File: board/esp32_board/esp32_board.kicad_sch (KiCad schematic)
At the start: 3 parts, among them J1 Screw_Terminal_01x19, J2 Screw_Terminal_01x19, U1 ESP32-DevKitC

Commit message: feat: Updated board
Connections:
- net 3V3: now reaches U1.1 (3V3)
- net 3V3: now also J2.1 (Pin_1)
- net 26: now reaches U1.10 (DAC_2/ADC2_CH9/GPIO26)
- net 26: now also J2.10 (Pin_10)
- net 27: now reaches U1.11 (ADC2_CH7/GPIO27)
- net 27: now also J2.11 (Pin_11)
- net 14: now reaches U1.12 (MTMS/GPIO14/ADC2_CH6)
- net 14: now also J2.12 (Pin_12)
- net 12: now reaches U1.13 (MTDI/GPIO12/ADC2_CH5)
- net 12: now also J2.13 (Pin_13)
- net GND: now reaches U1.14 (GND), U1.32 (GND), U1.38 (GND)
- net GND: now also J1.1 (Pin_1), J1.7 (Pin_7), J2.14 (Pin_14)
- net 13: now reaches U1.15 (MTCK/GPIO13/ADC2_CH4)
- net 13: now also J2.15 (Pin_15)
- net SD2: now reaches U1.16 (SD_DATA2/GPIO9)
- net SD2: now also J2.16 (Pin_16)
- net SD3: now reaches U1.17 (SD_DATA3/GPIO10)
- net SD3: now also J2.17 (Pin_17)
- net CMD: now reaches U1.18 (CMD)
- net CMD: now also J2.18 (Pin_18)
- net V5: now reaches U1.19 (5V)
- net V5: now also J2.19 (Pin_19)
- net EN: now reaches U1.2 (CHIP_PU)
- net EN: now also J2.2 (Pin_2)
- net CLK: now reaches U1.20 (SD_CLK/GPIO6)
- net CLK: now also J1.19 (Pin_19)
- net SD0: now reaches U1.21 (SD_DATA0/GPIO7)
- net SD0: now also J1.18 (Pin_18)
- net SD1: now reaches U1.22 (SD_DATA1/GPIO8)
- net SD1: now also J1.17 (Pin_17)
- net 15: now reaches U1.23 (MTDO/GPIO15/ADC2_CH3)
- net 15: now also J1.16 (Pin_16)
- net 2: now reaches U1.24 (ADC2_CH2/GPIO2)
- net 2: now also J1.15 (Pin_15)
- net 0: now reaches U1.25 (GPIO0/BOOT/ADC2_CH1)
- net 0: now also J1.14 (Pin_14)
- net 4: now reaches U1.26 (ADC2_CH0/GPIO4)
- net 4: now also J1.13 (Pin_13)
- net 16: now reaches U1.27 (GPIO16)
- net 16: now also J1.12 (Pin_12)
- net 17: now reaches U1.28 (GPIO17)
- net 17: now also J1.11 (Pin_11)
- net 5: now reaches U1.29 (GPIO5)
- net 5: now also J1.10 (Pin_10)
- net SP: now reaches U1.3 (SENSOR_VP/GPIO36/ADC1_CH0)
- net SP: now also J2.3 (Pin_3)
- net 18: now reaches U1.30 (GPIO18)
- net 18: now also J1.9 (Pin_9)
- net 19: now reaches U1.31 (GPIO19)
- net 19: now also J1.8 (Pin_8)
- net 21: now reaches U1.33 (GPIO21)
- net 21: now also J1.6 (Pin_6)
- net RX: now reaches U1.34 (U0RXD/GPIO3)
- net RX: now also J1.5 (Pin_5)
- net TX: now reaches U1.35 (U0TXD/GPIO1)
- net TX: now also J1.4 (Pin_4)
- net 22: now reaches U1.36 (GPIO22)
- net 22: now also J1.3 (Pin_3)
- net 23: now reaches U1.37 (GPIO23)
- net 23: now also J1.2 (Pin_2)
- net SN: now reaches U1.4 (SENSOR_VN/GPIO39/ADC1_CH3)
- net SN: now also J2.4 (Pin_4)
- net 34: now reaches U1.5 (VDET_1/GPIO34/ADC1_CH6)
- net 34: now also J2.5 (Pin_5)
- net 35: now reaches U1.6 (VDET_2/GPIO35/ADC1_CH7)
- net 35: now also J2.6 (Pin_6)
- net 32: now reaches U1.7 (32K_XP/GPIO32/ADC1_CH4)
- net 32: now also J2.7 (Pin_7)
- net 33: now reaches U1.8 (32K_XN/GPIO33/ADC1_CH5)
- net 33: now also J2.8 (Pin_8)
- net 25: now reaches U1.9 (DAC_1/ADC2_CH8/GPIO25)
- net 25: now also J2.9 (Pin_9)

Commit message: feat: Updated presentation and board
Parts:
- J1, J2: footprint (none) -> Connector_PinHeader_2.54mm:PinHeader_1x19_P2.54mm_Vertical
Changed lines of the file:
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@@
 			)
 		)
-		(property "Footprint" ""
+		(property "Footprint" "Connector_PinHeader_2.54mm:PinHeader_1x19_P2.54mm_Vertical"
 			(at 226.06 86.36 0)
 			(effects
@@
 			)
 		)
-		(property "Footprint" ""
+		(property "Footprint" "Connector_PinHeader_2.54mm:PinHeader_1x19_P2.54mm_Vertical"
 			(at 73.66 86.36 0)
 			(effects

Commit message: feat: Updated board
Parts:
- added J3, J5: Conn_01x19_Socket, Connector_PinSocket_2.54mm:PinSocket_1x19_P2.54mm_Vertical, symbol Connector:Conn_01x19_Socket
- added J4, J6: Conn_01x19_Pin, Connector_PinSocket_2.54mm:PinSocket_1x19_P2.54mm_Vertical, symbol Connector:Conn_01x19_Pin
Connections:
- net 0: now also J5.14 (Pin_14), J6.14 (Pin_14)
- net 12: now also J3.13 (Pin_13), J4.13 (Pin_13)
- net 13: now also J3.15 (Pin_15), J4.15 (Pin_15)
- net 14: now also J3.12 (Pin_12), J4.12 (Pin_12)
- net 15: now also J5.16 (Pin_16), J6.16 (Pin_16)
- net 16: now also J5.12 (Pin_12), J6.12 (Pin_12)
- net 17: now also J5.11 (Pin_11), J6.11 (Pin_11)
- net 18: now also J5.9 (Pin_9), J6.9 (Pin_9)
- net 19: now also J5.8 (Pin_8), J6.8 (Pin_8)
- net 2: now also J5.15 (Pin_15), J6.15 (Pin_15)
- net 21: now also J5.6 (Pin_6), J6.6 (Pin_6)
- net 22: now also J5.3 (Pin_3), J6.3 (Pin_3)
- net 23: now also J5.2 (Pin_2), J6.2 (Pin_2)
- net 25: now also J3.9 (Pin_9), J4.9 (Pin_9)
- net 26: now also J3.10 (Pin_10), J4.10 (Pin_10)
- net 27: now also J3.11 (Pin_11), J4.11 (Pin_11)
- net 32: now also J3.7 (Pin_7), J4.7 (Pin_7)
- net 33: now also J3.8 (Pin_8), J4.8 (Pin_8)
- net 34: now also J3.5 (Pin_5), J4.5 (Pin_5)
- net 35: now also J3.6 (Pin_6), J4.6 (Pin_6)
- net 3V3: now also J3.1 (Pin_1), J4.1 (Pin_1)
- net 4: now also J5.13 (Pin_13), J6.13 (Pin_13)
- net 5: now also J5.10 (Pin_10), J6.10 (Pin_10)
- net CLK: now also J5.19 (Pin_19), J6.19 (Pin_19)
- net CMD: now also J3.18 (Pin_18), J4.18 (Pin_18)
- net EN: now also J3.2 (Pin_2), J4.2 (Pin_2)
- net GND: now also J3.14 (Pin_14), J4.14 (Pin_14), J5.1 (Pin_1), J5.7 (Pin_7), J6.1 (Pin_1), J6.7 (Pin_7)
- net RX: now also J5.5 (Pin_5), J6.5 (Pin_5)
- net SD0: now also J5.18 (Pin_18), J6.18 (Pin_18)
- net SD1: now also J5.17 (Pin_17), J6.17 (Pin_17)
- net SD2: now also J3.16 (Pin_16), J4.16 (Pin_16)
- net SD3: now also J3.17 (Pin_17), J4.17 (Pin_17)
- net SN: now also J3.4 (Pin_4), J4.4 (Pin_4)
- net SP: now also J3.3 (Pin_3), J4.3 (Pin_3)
- net TX: now also J5.4 (Pin_4), J6.4 (Pin_4)
- net V5: now also J3.19 (Pin_19), J4.19 (Pin_19)
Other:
- moved on the sheet: J1, J2

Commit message: feat: Updated board and presentation
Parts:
- added H1, H2, H3: MountingHole, symbol Mechanical:MountingHole
- added K1, K2, K3: Relay_SPST-NO, symbol Relay:Relay_SPST-NO
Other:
- moved on the sheet: J1, J2, J3, J4, J5, J6, U1

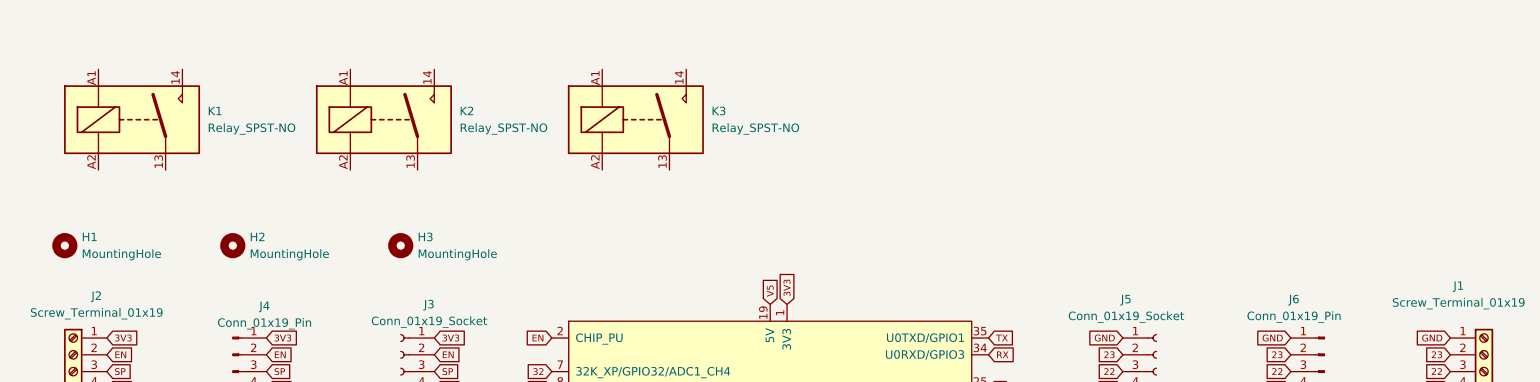
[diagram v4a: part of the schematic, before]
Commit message: feat(board): Added modules - gps, compass, relay. And builded schematic
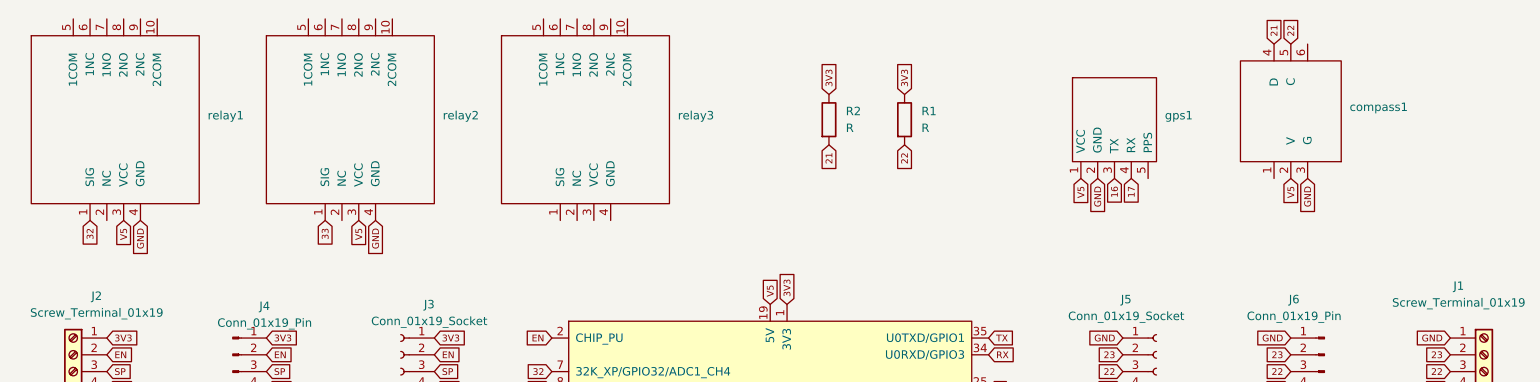
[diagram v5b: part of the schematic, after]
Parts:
- removed H1, H2, H3: MountingHole, symbol Mechanical:MountingHole
- removed K1, K2, K3: Relay_SPST-NO, symbol Relay:Relay_SPST-NO
- added R1, R2: R, symbol Device:R
- added compass1: ~, symbol slon_modules:compass
- added gps1: ~, symbol slon_modules:gps
- added relay1, relay2, relay3: ~, symbol slon_modules:relay
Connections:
- net 16: now also gps1.3 (TX)
- net 17: now also gps1.4 (RX)
- net 21: now also R2.2, compass1.4 (D)
- net 22: now also R1.2, compass1.5 (C)
- net 32: now also relay1.1 (SIG)
- net 33: now also relay2.1 (SIG)
- net 3V3: now also R1.1, R2.1
- net GND: now also compass1.3 (G), gps1.2 (GND), relay1.4 (GND), relay2.4 (GND)
- net V5: now also compass1.2 (V), gps1.1 (VCC), relay1.3 (VCC), relay2.3 (VCC)

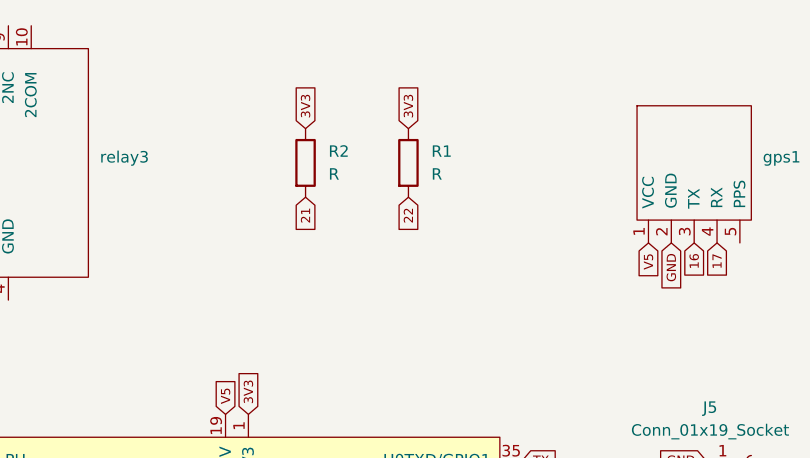
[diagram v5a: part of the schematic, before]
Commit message: feat(docs): Added board schematic into docs
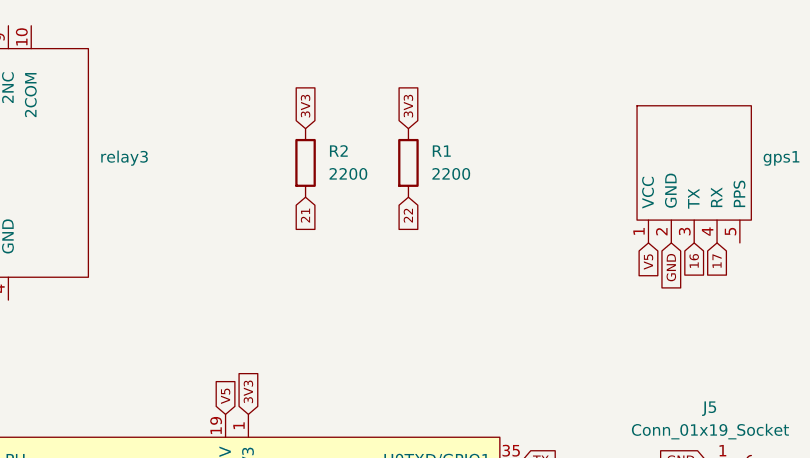
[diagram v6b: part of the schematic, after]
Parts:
- R1, R2: value R -> 2200
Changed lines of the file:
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@@
 			)
 		)
-		(property "Value" "R"
+		(property "Value" "2200"
 			(at 154.94 33.0199 0)
 			(effects
@@
 			)
 		)
-		(property "Value" "R"
+		(property "Value" "2200"
 			(at 143.51 33.0199 0)
 			(effects

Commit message: feat: Updated docs and board
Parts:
- compass1: footprint (none) -> slon_modules:compass
- gps1: footprint (none) -> slon_modules:gps
- relay1, relay2, relay3: footprint (none) -> slon_modules:relay
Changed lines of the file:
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@@
 			)
 		)
-		(property "Footprint" ""
+		(property "Footprint" "slon_modules:compass"
 			(at 210.82 38.1 0)
 			(effects
@@
 			)
 		)
-		(property "Footprint" ""
+		(property "Footprint" "slon_modules:relay"
 			(at 104.14 44.45 0)
 			(effects
@@
 			)
 		)
-		(property "Footprint" ""
+		(property "Footprint" "slon_modules:relay"
 			(at 33.02 44.45 0)
 			(effects
@@
 			)
 		)
-		(property "Footprint" ""
+		(property "Footprint" "slon_modules:relay"
 			(at 68.58 44.45 0)
 			(effects
@@
 			)
 		)
-		(property "Footprint" ""
+		(property "Footprint" "slon_modules:gps"
 			(at 177.8 38.1 0)
 			(effects

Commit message: feat(board): Added roads
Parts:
- J3, J5: footprint Connector_PinSocket_2.54mm:PinSocket_1x19_P2.54mm_Vertical -> Connector_PinHeader_2.54mm:PinHeader_1x19_P2.54mm_Vertical
- R1, R2: footprint (none) -> slon_modules:r
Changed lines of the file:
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@@
 			)
 		)
-		(property "Footprint" ""
+		(property "Footprint" "slon_modules:r"
 			(at 150.622 31.75 90)
 			(effects
@@
 			)
 		)
-		(property "Footprint" "Connector_PinSocket_2.54mm:PinSocket_1x19_P2.54mm_Vertical"
+		(property "Footprint" "Connector_PinHeader_2.54mm:PinHeader_1x19_P2.54mm_Vertical"
 			(at 190.5 87.63 0)
 			(effects
@@
 			)
 		)
-		(property "Footprint" ""
+		(property "Footprint" "slon_modules:r"
 			(at 139.192 31.75 90)
 			(effects
@@
 			)
 		)
-		(property "Footprint" "Connector_PinSocket_2.54mm:PinSocket_1x19_P2.54mm_Vertical"
+		(property "Footprint" "Connector_PinHeader_2.54mm:PinHeader_1x19_P2.54mm_Vertical"
 			(at 76.2 87.63 0)
 			(effects
